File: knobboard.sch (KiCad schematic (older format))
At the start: 1 part

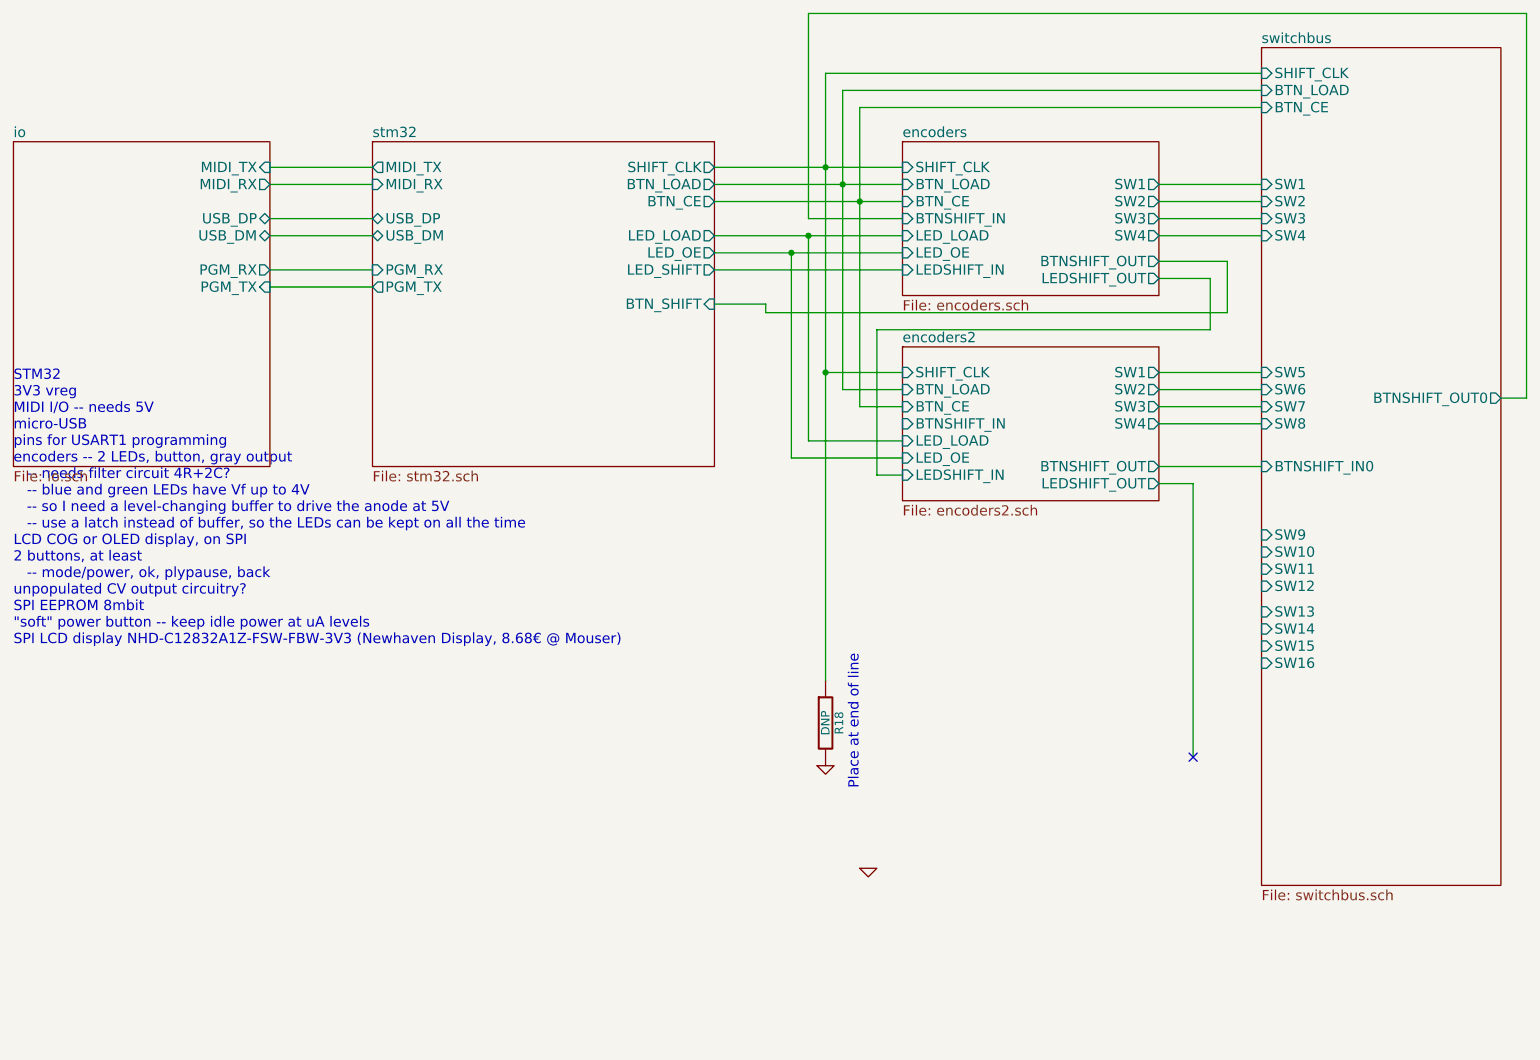
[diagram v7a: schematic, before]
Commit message: Add holes
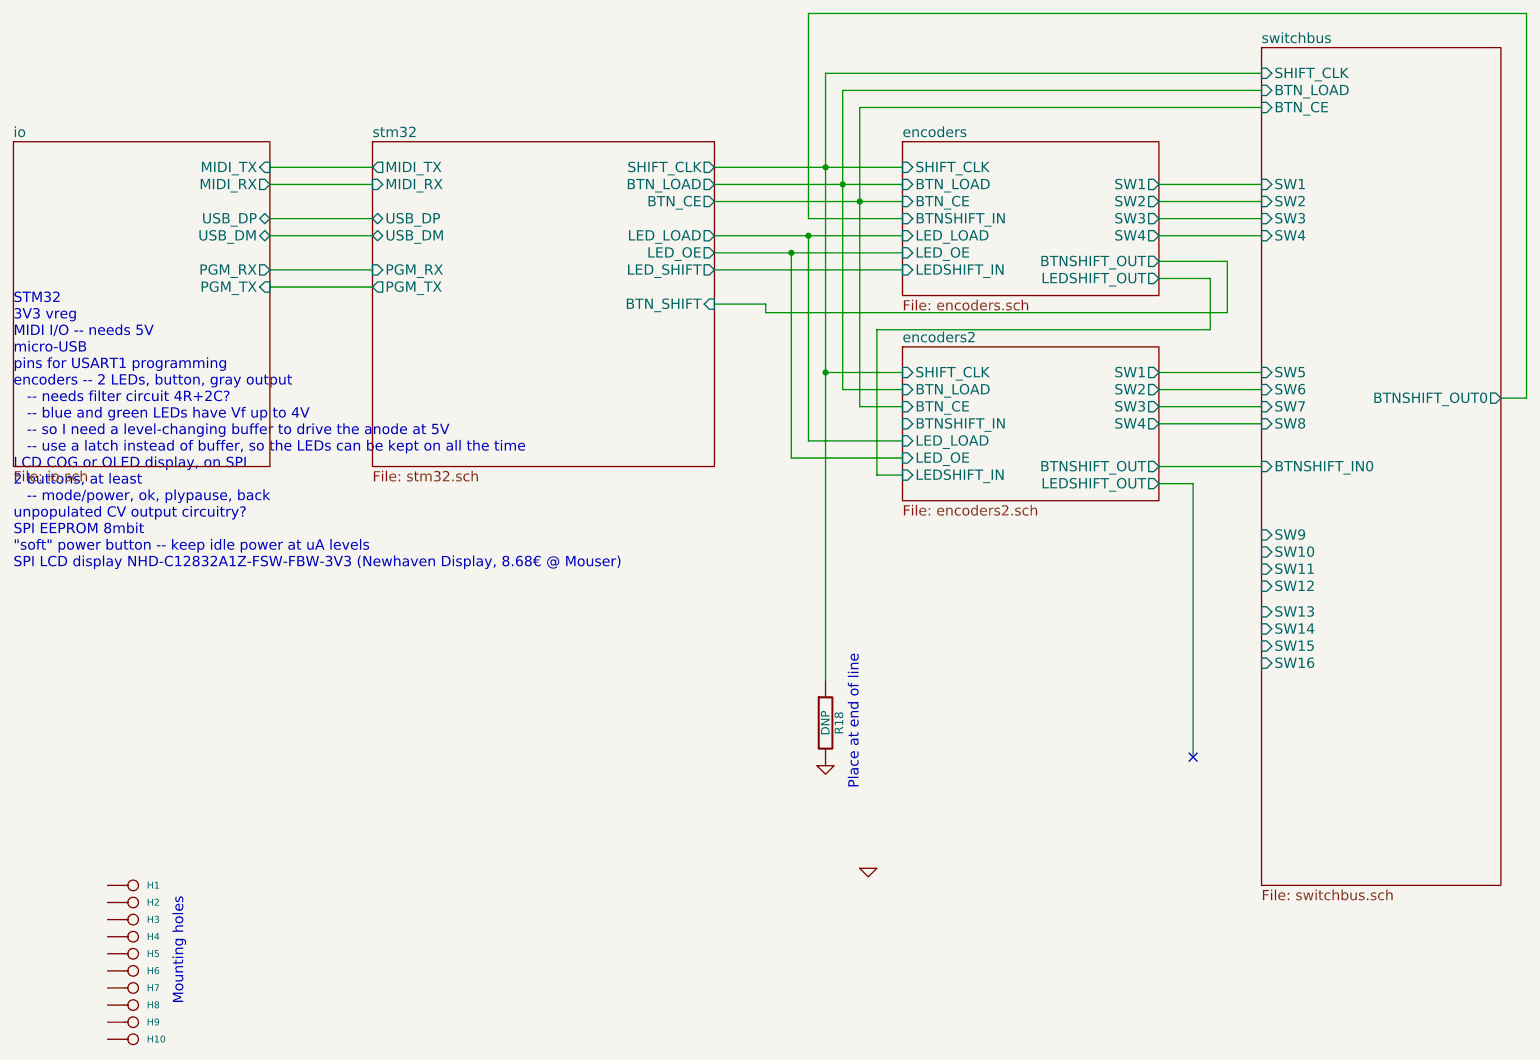
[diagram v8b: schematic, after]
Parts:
- added H1, H10, H2, H3, H4, H5, H6, H7, H8, H9: CONN_1, symbol CONN_1
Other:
- note added: "Mounting holes"
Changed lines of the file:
@@
-EESchema Schematic File Version 2  date Thu 19 Apr 2012 10:08:52 PM CEST
+EESchema Schematic File Version 2  date Fri 20 Apr 2012 08:02:00 AM CEST
 LIBS:power
 LIBS:device
@@
 Sheet 1 6
 Title ""
-Date "19 apr 2012"
+Date "20 apr 2012"
 Rev ""
 Comp ""
@@
 Comment4 ""
 $EndDescr
+$Comp
+L CONN_1 H10
+U 1 1 4F90F9F5
+P 2200 6800
+F 0 "H10" H 2280 6800 40  0000 L CNN
+F 1 "CONN_1" H 2200 6855 30  0001 C CNN
+	1    2200 6800
+	1    0    0    -1
+$EndComp
+$Comp
+L CONN_1 H9
+U 1 1 4F90F9F3
+P 2200 6700
+F 0 "H9" H 2280 6700 40  0000 L CNN
+F 1 "CONN_1" H 2200 6755 30  0001 C CNN
+	1    2200 6700
+	1    0    0    -1
+$EndComp
+Text Notes 2500 6600 1    60   ~ 0
+Mounting holes
+$Comp
+L CONN_1 H8
+U 1 1 4F90F606
+P 2200 6600
+F 0 "H8" H 2280 6600 40  0000 L CNN
+F 1 "CONN_1" H 2200 6655 30  0001 C CNN
+	1    2200 6600
+	1    0    0    -1
+$EndComp
+$Comp
+L CONN_1 H7
+U 1 1 4F90F605
+P 2200 6500
+F 0 "H7" H 2280 6500 40  0000 L CNN
+F 1 "CONN_1" H 2200 6555 30  0001 C CNN
+	1    2200 6500
+	1    0    0    -1
+$EndComp
+$Comp
+L CONN_1 H6
+U 1 1 4F90F604
+P 2200 6400
+F 0 "H6" H 2280 6400 40  0000 L CNN
+F 1 "CONN_1" H 2200 6455 30  0001 C CNN
+	1    2200 6400
+	1    0    0    -1
+$EndComp
+$Comp
+L CONN_1 H5
+U 1 1 4F90F602
+P 2200 6300
+F 0 "H5" H 2280 6300 40  0000 L CNN
+F 1 "CONN_1" H 2200 6355 30  0001 C CNN
+	1    2200 6300
+	1    0    0    -1
+$EndComp
+$Comp
+L CONN_1 H4
+U 1 1 4F90F601
+P 2200 6200
+F 0 "H4" H 2280 6200 40  0000 L CNN
+F 1 "CONN_1" H 2200 6255 30  0001 C CNN
+	1    2200 6200
+	1    0    0    -1
+$EndComp
+$Comp
+L CONN_1 H3
+U 1 1 4F90F5FF
+P 2200 6100
+F 0 "H3" H 2280 6100 40  0000 L CNN
+F 1 "CONN_1" H 2200 6155 30  0001 C CNN
+	1    2200 6100
+	1    0    0    -1
+$EndComp
+$Comp
+L CONN_1 H2
+U 1 1 4F90F5FD
+P 2200 6000
+F 0 "H2" H 2280 6000 40  0000 L CNN
+F 1 "CONN_1" H 2200 6055 30  0001 C CNN
+	1    2200 6000
+	1    0    0    -1
+$EndComp
+$Comp
+L CONN_1 H1
+U 1 1 4F90F5D6
+P 2200 5900
+F 0 "H1" H 2280 5900 40  0000 L CNN
+F 1 "CONN_1" H 2200 5955 30  0001 C CNN
+	1    2200 5900
+	1    0    0    -1
+$EndComp
 Connection ~ 6050 2200
 Wire Wire Line
@@
 F14 "SHIFT_CLK" O R 5600 1700 60
 $EndSheet
-Text Notes 1500 4500 0    60   ~ 0
+Text Notes 1500 4050 0    60   ~ 0
 STM32\n3V3 vreg\nMIDI I/O -- needs 5V\nmicro-USB\npins for USART1 programming\nencoders -- 2 LEDs, button, gray output\n   -- needs filter circuit 4R+2C?\n   -- blue and green LEDs have Vf up to 4V\n   -- so I need a level-changing buffer to drive the anode at 5V\n   -- use a latch instead of buffer, so the LEDs can be kept on all the time\nLCD COG or OLED display, on SPI\n2 buttons, at least\n   -- mode/power, ok, plypause, back\nunpopulated CV output circuitry?\nSPI EEPROM 8mbit\n"soft" power button -- keep idle power at uA levels\nSPI LCD display NHD-C12832A1Z-FSW-FBW-3V3 (Newhaven Display, 8.68€ @ Mouser)
 $EndSCHEMATC
